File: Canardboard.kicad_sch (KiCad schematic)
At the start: 51 parts, among them J5 Conn_01x03_Male, J6 Conn_01x03_Male, J7 Conn_01x03_Male, U1 ESP32-S3, Y1 40MHz±10ppm

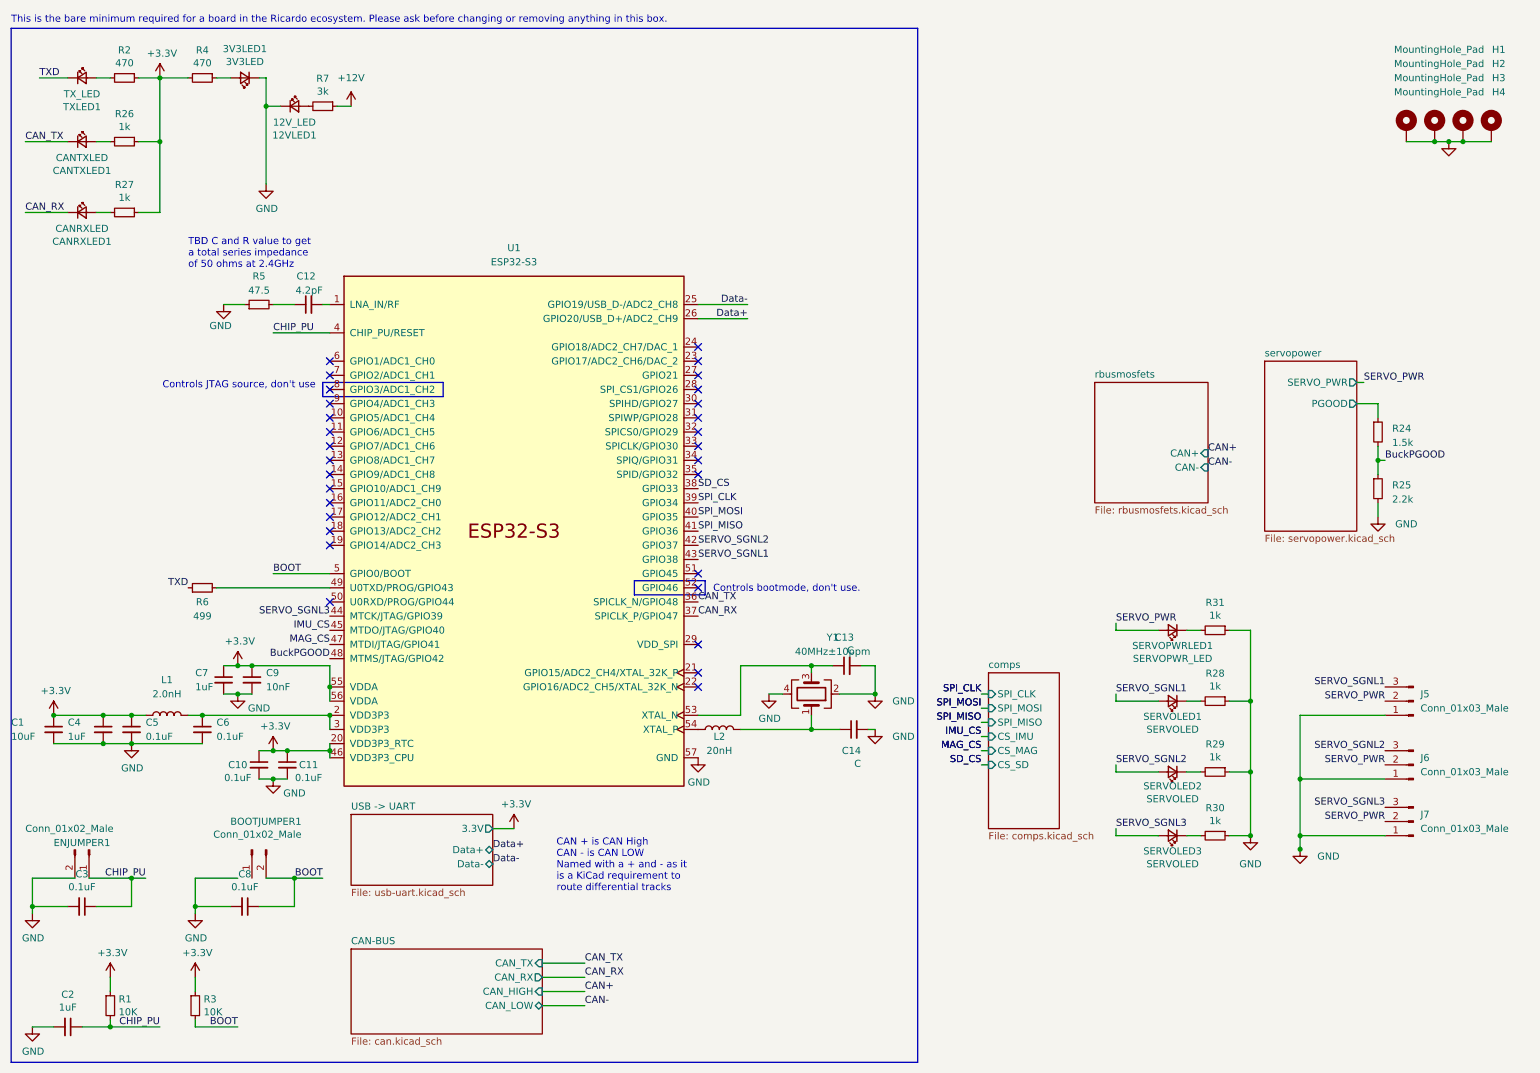
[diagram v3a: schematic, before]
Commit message: schematic review updated
fixed:
-pin 1 on the bootjumper is missing a connection. 
- Move the SD card to a 2nd SPI bus (so a 2nd set of MISO, MOSI, SCLK) as the rest of the bus is blocked while data is written to it, which would interrupt sensor readings. 
- Add a pull-up resistor on the DET_A pin of the micro SD card, and also connect that pin to the esp32 (picture from pickle) 
- VDD on the IMU (U7) is not connected to any power, should be connected to 3.3V 
- Turns out CAN capacitors C18, C19 actually aren’t needed. It’s up to you if you want to keep them, but if you do keep them could you change their value to “DNP” (stands for Do not place) 
-  Add test points to lines which can potentially cause issues. Most of the time this just means places that are connected to the ESP32, but especially places like the SPI lines (including chip selects). Also, add test points to TXD and RXD on the esp32 in case we have to solder to them for programming  

Servo Buck Converter 
- Pin 29 missing ground connection 
-  Add a text label with the part number of the 2.1uH inductor 

LTC4412s 
- No power net connected to Vin 
- stocky diodes replaced logic mosfets
- switched mosfets around so S is common
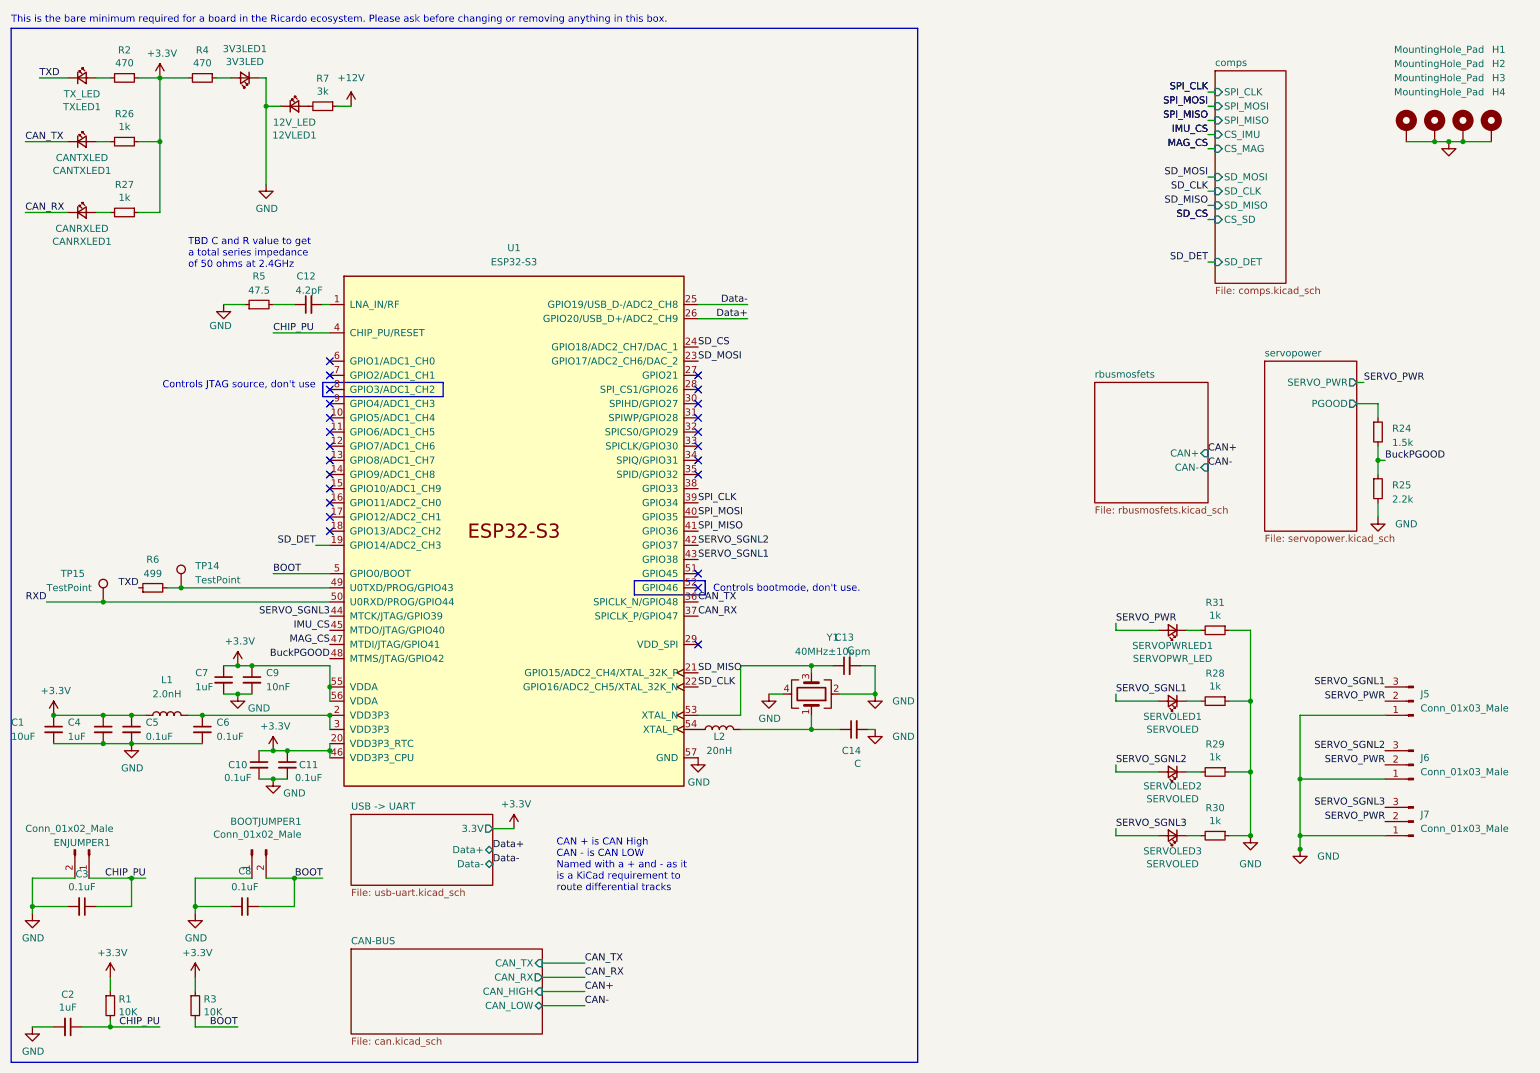
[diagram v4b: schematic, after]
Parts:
- added TP14, TP15: TestPoint, symbol Connector:TestPoint
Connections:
- net GND: now also BOOTJUMPER1.1 (Pin_1)
- net SD_CS: now also U1.24 (GPIO18/ADC2_CH7/DAC_1); no longer U1.38 (GPIO33)
- net SD_DET: now reaches U1.19 (GPIO14/ADC2_CH3)
- net SD_MISO: now reaches U1.21 (GPIO15/ADC2_CH4/XTAL_32K_P)
- net SD_CLK: now reaches U1.22 (GPIO16/ADC2_CH5/XTAL_32K_N)
- net SD_MOSI: now reaches U1.23 (GPIO17/ADC2_CH6/DAC_2)
- net at R6.2, U1.49 (U0TXD/PROG/GPIO43): now also TP14.1
- net RXD: now reaches U1.50 (U0RXD/PROG/GPIO44)
- net RXD: now also TP15.1
- no-connect marks 30 -> 24
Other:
- sheet comps ports: added SD_CLK, SD_DET, SD_MISO, SD_MOSI; removed none
- moved on the sheet: R6

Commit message: I don't want to lose all my changes so I will commit, commit.
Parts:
- TP14, TP15: footprint (none) -> TestPoint:TestPoint_Pad_D1.0mm
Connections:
- net CAN_RX: now also U1.42 (GPIO37); no longer U1.37 (SPICLK_P/GPIO47)
- net CAN_TX: now also U1.41 (GPIO36); no longer U1.36 (SPICLK_N/GPIO48)
- net IMU_CS: now also U1.38 (GPIO33); no longer U1.45 (MTDO/JTAG/GPIO40)
- net MAG_CS: now also U1.37 (SPICLK_P/GPIO47); no longer U1.47 (MTDI/JTAG/GPIO41)
- net SERVO_SGNL2: now also U1.45 (MTDO/JTAG/GPIO40); no longer U1.42 (GPIO37)
- net SPI_MISO: now also U1.36 (SPICLK_N/GPIO48); no longer U1.41 (GPIO36)
- net TXD: now also TP14.1
- net at R6.2, U1.49 (U0TXD/PROG/GPIO43): no longer TP14.1
- no-connect marks 24 -> 25
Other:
- moved on the sheet: TP14

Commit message: First PCB layout draft
I need to learn how to properly do fills
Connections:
- net SERVO_SGNL2: now also U1.44 (MTCK/JTAG/GPIO39); no longer U1.45 (MTDO/JTAG/GPIO40)
- net SERVO_SGNL3: now also U1.45 (MTDO/JTAG/GPIO40); no longer U1.44 (MTCK/JTAG/GPIO39)
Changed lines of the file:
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@@
     (effects (font (size 1.27 1.27)) (justify left bottom))
-  )
-  (label "SERVO_SGNL3" (at 69.85 118.11 180) (fields_autoplaced)
-    (effects (font (size 1.27 1.27)) (justify right bottom))
-  )
-  (label "SERVO_SGNL2" (at 69.85 120.65 180) (fields_autoplaced)
-    (effects (font (size 1.27 1.27)) (justify right bottom))
   )
   (label "SERVO_SGNL3" (at 210.82 156.21 0) (fields_autoplaced)
@@
     (effects (font (size 1.27 1.27)) (justify right bottom))
   )
+  (label "SERVO_SGNL3" (at 69.85 120.65 180) (fields_autoplaced)
+    (effects (font (size 1.27 1.27)) (justify right bottom))
+  )
   (label "BOOT" (at 68.58 165.1 180) (fields_autoplaced)
     (effects (font (size 1.27 1.27)) (justify right bottom))
@@
     (effects (font (size 1.27 1.27)) (justify left bottom))
   )
+  (label "SERVO_SGNL2" (at 69.85 118.11 180) (fields_autoplaced)
+    (effects (font (size 1.27 1.27)) (justify right bottom))
+  )
   (label "SPI_MISO" (at 227.33 29.21 180) (fields_autoplaced)

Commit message: fixed all of andrei's comments v1
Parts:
- U1: footprint Package_DFN_QFN:QFN-56-1EP_7x7mm_P0.4mm_EP5.6x5.6mm -> iclr:QFN40P700X700X90-57N
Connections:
- net SERVOBUCK_EN: now reaches U1.14 (GPIO9/ADC1_CH8)
- no-connect marks 25 -> 24
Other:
- sheet servopower ports: added SERVOBUCK_EN; removed none
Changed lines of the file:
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@@
   (no_connect (at 69.85 72.39))
   (no_connect (at 69.85 123.19))
-  (no_connect (at 69.85 92.71))
   (no_connect (at 69.85 77.47))
   (no_connect (at 135.89 82.55))
@@
     (effects (font (size 1.27 1.27)) (justify left bottom))
   )
+  (label "SERVOBUCK_EN" (at 69.85 92.71 180) (fields_autoplaced)
+    (effects (font (size 1.27 1.27)) (justify right bottom))
+  )
   (label "SPI_CLK" (at 227.33 24.13 180) (fields_autoplaced)
     (effects (font (size 1.27 1.27)) (justify right bottom))
@@
   (label "SPI_CLK" (at 227.33 24.13 180) (fields_autoplaced)
     (effects (font (size 1.27 1.27)) (justify right bottom))
+  )
+  (label "SERVOBUCK_EN" (at 254 109.22 0) (fields_autoplaced)
+    (effects (font (size 1.27 1.27)) (justify left bottom))
   )
   (label "SERVO_SGNL2" (at 210.82 144.78 0) (fields_autoplaced)
@@
       (effects (font (size 1.27 1.27)))
     )
-    (property "Footprint" "Package_DFN_QFN:QFN-56-1EP_7x7mm_P0.4mm_EP5.6x5.6mm" (at 102.87 153.67 0)
+    (property "Footprint" "iclr:QFN40P700X700X90-57N" (at 102.87 153.67 0)
       (effects (font (size 1.27 1.27)) hide)
     )
@@
     )
   )
-  (sheet (at 237.49 72.39) (size 16.51 30.48) (fields_autoplaced)
+  (sheet (at 237.49 72.39) (size 16.51 45.72) (fields_autoplaced)
     (stroke (width 0.1524) (type solid))
     (fill (color 0 0 0 0.0000))
@@
       (effects (font (size 1.27 1.27)) (justify left bottom))
     )
-    (property "Sheetfile" "servopower.kicad_sch" (at 237.49 103.4546 0)
+    (property "Sheetfile" "servopower.kicad_sch" (at 237.49 118.6946 0)
       (effects (font (size 1.27 1.27)) (justify left top))
     )
@@
       (effects (font (size 1.27 1.27)) (justify right))
     )
+    (pin "SERVOBUCK_EN" input (at 254 109.22 0)
+      (effects (font (size 1.27 1.27)) (justify right))
+    )

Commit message: did some stuffus
added a new power plane in servo power on the back side
made SW larger
and a lot more changes
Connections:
- net SERVOBUCK_EN: now also U1.44 (MTCK/JTAG/GPIO39); no longer U1.14 (GPIO9/ADC1_CH8)
- net SERVO_SGNL2: now also U1.14 (GPIO9/ADC1_CH8); no longer U1.44 (MTCK/JTAG/GPIO39)
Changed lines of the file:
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@@
     (effects (font (size 1.27 1.27)) (justify left bottom))
+  )
+  (label "SERVO_SGNL2" (at 69.85 92.71 180) (fields_autoplaced)
+    (effects (font (size 1.27 1.27)) (justify right bottom))
   )
   (label "SERVO_PWR" (at 255.27 76.2 0) (fields_autoplaced)
@@
   (label "SERVO_SGNL1" (at 135.89 107.95 0) (fields_autoplaced)
     (effects (font (size 1.27 1.27)) (justify left bottom))
-  )
-  (label "SERVOBUCK_EN" (at 69.85 92.71 180) (fields_autoplaced)
-    (effects (font (size 1.27 1.27)) (justify right bottom))
   )
   (label "SPI_CLK" (at 227.33 24.13 180) (fields_autoplaced)
@@
   (label "MAG_CS" (at 135.89 118.11 0) (fields_autoplaced)
     (effects (font (size 1.27 1.27)) (justify left bottom))
-  )
-  (label "SERVO_SGNL2" (at 69.85 118.11 180) (fields_autoplaced)
-    (effects (font (size 1.27 1.27)) (justify right bottom))
   )
   (label "SPI_MISO" (at 227.33 29.21 180) (fields_autoplaced)
@@
     (effects (font (size 1.27 1.27)) (justify right bottom))
   )
+  (label "SERVOBUCK_EN" (at 69.85 118.11 180) (fields_autoplaced)
+    (effects (font (size 1.27 1.27)) (justify right bottom))
+  )
